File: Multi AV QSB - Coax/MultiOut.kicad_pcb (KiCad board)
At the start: 2 copper layers, 22 x 22.4 mm, 7 parts, among them J1 Multi AV, J2 R, J3 G, J4 B

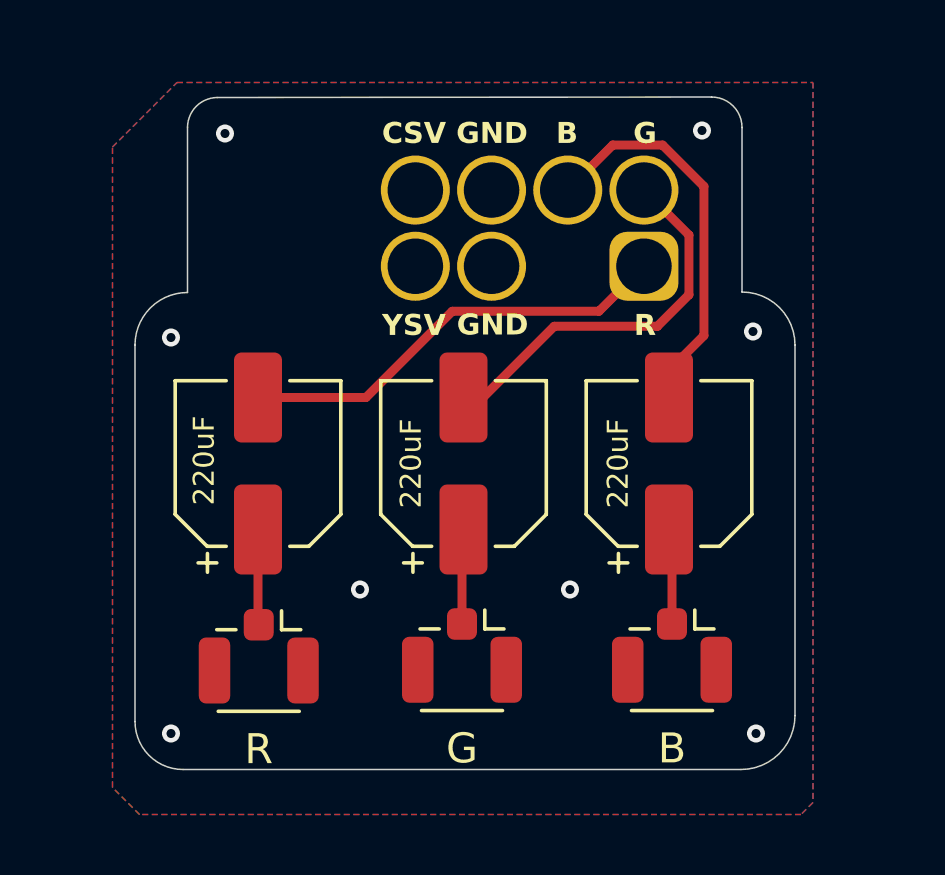
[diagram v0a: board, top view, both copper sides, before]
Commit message: QSB - remove AC coupling and add GND lift jumper
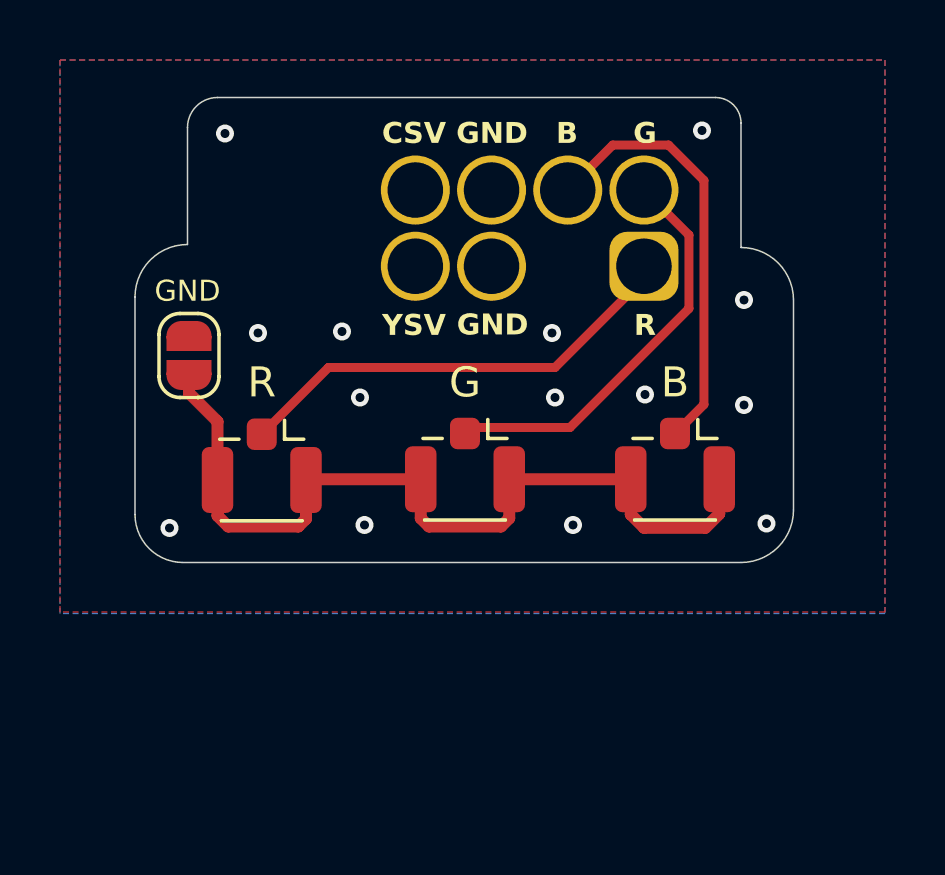
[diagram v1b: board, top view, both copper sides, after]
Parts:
- removed C1, C2, C3: 220uF, Capacitor_SMD:CP_Elec_5x5.8
- added JP1: GND, Jumper:SolderJumper-2_P1.3mm_Open_RoundedPad1.0x1.5mm, F.Cu at (131.8, 87.1)
- moved J2 6.35 mm to (134.2, 90.8)
- moved J3 6.35 mm to (141.0, 90.8)
- moved J4 6.35 mm to (148.0, 90.8)
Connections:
- J1 pad 1: Net-(J1-Pin_1) -> /R
- J1 pad 2: Net-(J1-Pin_2) -> /G
- J1 pad 4: Net-(J1-Pin_4) -> /B
- J2 pad 2: GND -> Net-(J2-Ext)
- J3 pad 2: GND -> Net-(J2-Ext)
- J4 pad 2: GND -> Net-(J2-Ext)
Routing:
- net Net-(J2-Ext): track 0.00 -> 28.9 mm
- net Net-(J1-Pin_1): track 14.7 -> 0.00 mm
- net Net-(J1-Pin_4): track 13.3 -> 0.00 mm
- net Net-(J1-Pin_2): track 13.0 -> 0.00 mm
- net /R: track 3.19 -> 15.3 mm
- net /B: track 3.19 -> 14.5 mm
- net /G: track 3.17 -> 13.8 mm
- net GND: vias 8 -> 14
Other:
- board size 22 x 22.4 mm -> 21.9 x 15.5 mm
